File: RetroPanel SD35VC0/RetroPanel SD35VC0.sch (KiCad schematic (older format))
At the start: 20 parts, among them J1 Front Panel, J2 SD35VC0, J3 IDE, J4 GND, J5 +5V, J7 POWER, M1 Mounting_Pin, M10 Mounting_Pad, M11 Mounting_Pad, M12 Mounting_Pad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

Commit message: SD35VC0 Front sketched out
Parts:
- added J10: LED_POWER, RetroPanel:PinHeader_1x02_P2.54mm_Vertical, symbol Connector_Generic:Conn_01x02
- added J6: SW_TURBO, RetroPanel:PinHeader_1x02_P2.54mm_Vertical, symbol Connector_Generic:Conn_01x02
- added J8: LED_TURBO, RetroPanel:PinHeader_1x02_P2.54mm_Vertical, symbol Connector_Generic:Conn_01x02
- added J9: SW_POWER, RetroPanel:PinHeader_1x02_P2.54mm_Vertical, symbol Connector_Generic:Conn_01x02
- added R1, R2: 0, resistor:R_Axial_DIN0207_L6.3mm_D2.5mm_P10.16mm_Horizontal, symbol Device:R_Small
- J1: footprint RetroPanel:Module_Panel -> RetroPanel:SD35VC0_Module_Panel; symbol RetroPanel:Front_Panel -> RetroPanel:SD35VC0_Front_Panel
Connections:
- net LED_HDD1 is gone; now on net LED_TURBO1: J1.22 (LED_TURBO1)
- net LED_HDD2 is gone; now on net LED_TURBO2: J1.23 (LED_TURBO2)
- net SW_EXTRA1 is gone; now on net SW_TURBO1: J1.24 (SW_TURBO1)
- net SW_EXTRA2 is gone; now on net SW_TURBO2: J1.25 (SW_TURBO2)
- net SW_RESET1 is gone; now on net LED_PWR1: J1.8 (LED_PWR1)
- net SW_RESET2 is gone; now on net LED_PWR2: J1.9 (LED_PWR2)
- net +5V: now also J1.30 (VCC), J5.1 (Pin_1), J7.4 (Pin_4); no longer J1.1 (VCC)
- net GND: now also J1.1 (GND); no longer J1.30 (GND)
- net LED_PWR1: now also R2.2; no longer J1.6 (LED_PWR1)
- net LED_PWR2: now also J10.2 (Pin_2); no longer J1.7 (LED_PWR2)
- net LED_TURBO1: now also R1.2; no longer J1.28 (LED_TURBO1)
- net LED_TURBO2: now also J8.2 (Pin_2); no longer J1.29 (LED_TURBO2)
- net SW_PWR1: now also J1.6 (SW_PWR1), J9.1 (Pin_1); no longer J1.4 (SW_PWR1)
- net SW_PWR2: now also J1.7 (SW_PWR2), J9.2 (Pin_2); no longer J1.5 (SW_PWR2)
- net SW_TURBO1: now also J6.1 (Pin_1); no longer J1.26 (SW_TURBO1)
- net SW_TURBO2: now also J6.2 (Pin_2); no longer J1.27 (SW_TURBO2)
- new net: J8.1 (Pin_1), R1.1
- new net: J10.1 (Pin_1), R2.1
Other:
- moved on the sheet: J2, J3, J4, J5, J7

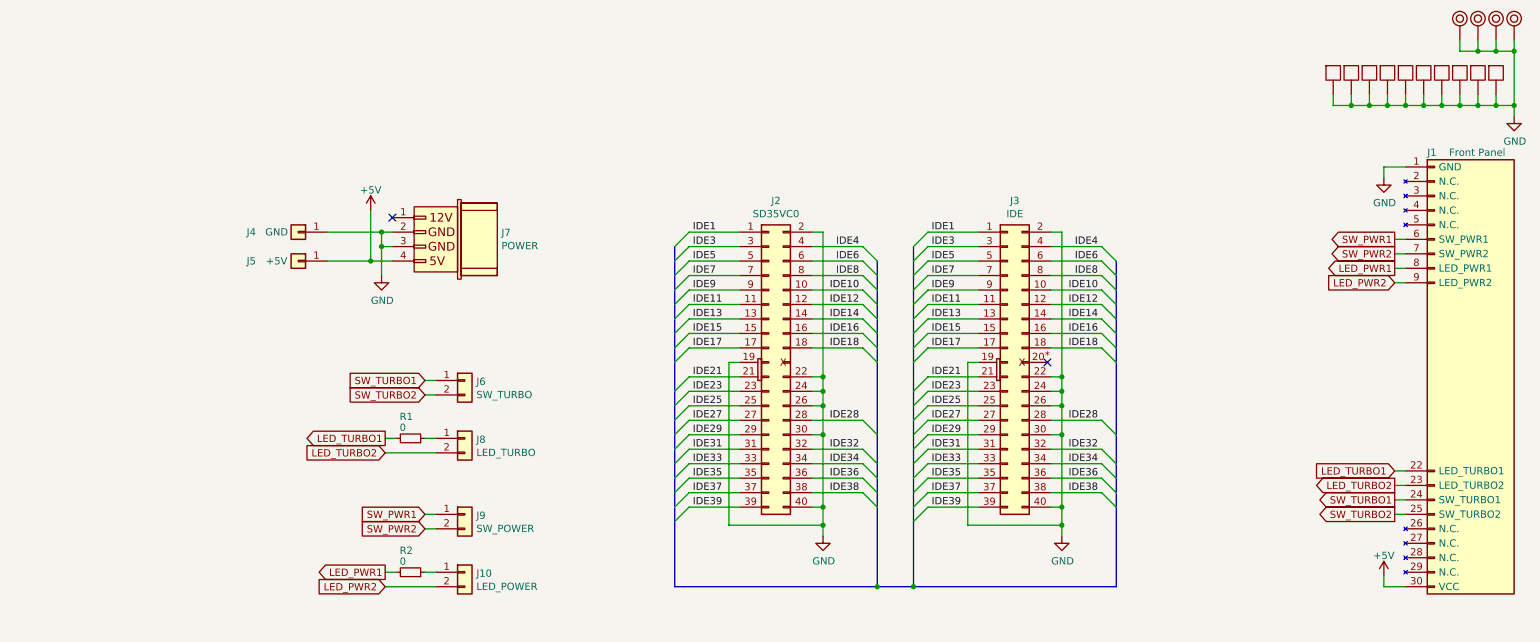
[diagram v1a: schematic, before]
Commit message: Changed SW_PWR to pads for cable as it probably should be
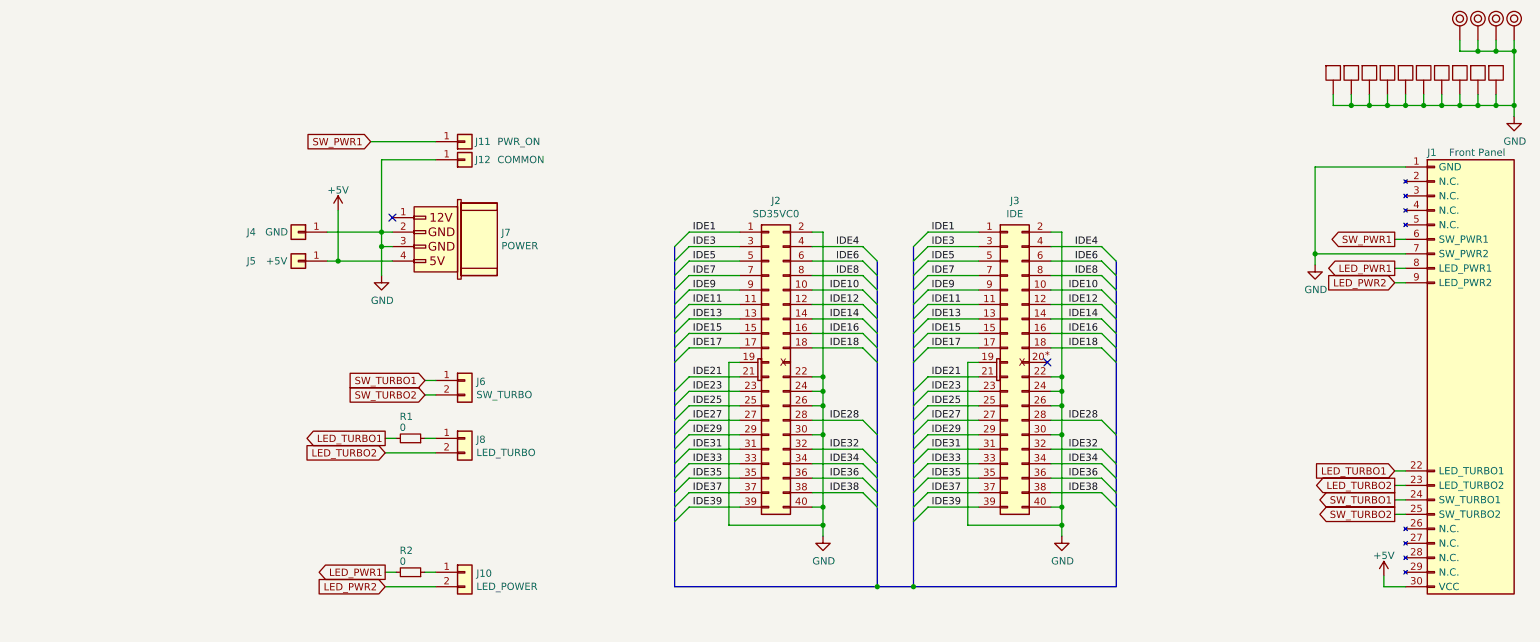
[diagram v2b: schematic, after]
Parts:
- removed J9: SW_POWER, RetroPanel:PinHeader_1x02_P2.54mm_Vertical, symbol Connector_Generic:Conn_01x02
- added J11: PWR_ON, RetroPanel:PSU_Wire, symbol Connector_Generic:Conn_01x01
- added J12: COMMON, RetroPanel:PSU_Wire, symbol Connector_Generic:Conn_01x01
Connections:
- net SW_PWR2 is gone; now on net GND: J1.7 (SW_PWR2)
- net GND: now also J12.1 (Pin_1)
- net SW_PWR1: now also J11.1 (Pin_1)
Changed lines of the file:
@@
 L power:GND #PWR0101
 U 1 1 6282785A
-P 10175 1725
-F 0 "#PWR0101" H 10175 1475 50  0001 C CNN
-F 1 "GND" H 10180 1552 50  0000 C CNN
-F 2 "" H 10175 1725 50  0001 C CNN
-F 3 "" H 10175 1725 50  0001 C CNN
-	1    10175 1725
+P 9700 2325
+F 0 "#PWR0101" H 9700 2075 50  0001 C CNN
+F 1 "GND" H 9705 2152 50  0000 C CNN
+F 2 "" H 9700 2325 50  0001 C CNN
+F 3 "" H 9700 2325 50  0001 C CNN
+	1    9700 2325
 	1    0    0    -1
 $EndComp
 Wire Wire Line
 	10175 4475 10175 4550
-Wire Wire Line
-	10175 1650 10175 1725
 Text GLabel 10250 2150 0    50   Output ~ 0
 SW_PWR1
-Text GLabel 10250 2250 0    50   Output ~ 0
-SW_PWR2
 Text GLabel 10250 2350 0    50   Output ~ 0
 LED_PWR1
@@
 Text GLabel 10250 3850 0    50   Output ~ 0
 LED_TURBO2
-Wire Wire Line
-	10250 2150 10325 2150
-Wire Wire Line
-	10250 2250 10325 2250
-Wire Wire Line
-	10250 2350 10325 2350
-Wire Wire Line
-	10250 2450 10325 2450
 Wire Wire Line
 	10250 3950 10325 3950
@@
 Connection ~ 3250 2100
 Wire Wire Line
-	2875 2300 3175 2300
-Wire Wire Line
-	10175 1650 10325 1650
+	2875 2300 2950 2300
 $Comp
 L RetroPanel:SD35VC0_Front_Panel J1
@@
 Wire Wire Line
 	3550 3525 3625 3525
-Text GLabel 3550 4050 0    50   Input ~ 0
+Text GLabel 3175 1475 0    50   Input ~ 0
 SW_PWR1
-Text GLabel 3550 4150 0    50   Input ~ 0
-SW_PWR2
-$Comp
-L Connector_Generic:Conn_01x02 J9
-U 1 1 635DD778
-P 3825 4050
-F 0 "J9" H 3905 4042 50  0000 L CNN
-F 1 "SW_POWER" H 3905 3951 50  0000 L CNN
-F 2 "RetroPanel:PinHeader_1x02_P2.54mm_Vertical" H 3825 4050 50  0001 C CNN
-F 3 "~" H 3825 4050 50  0001 C CNN
-	1    3825 4050
-	1    0    0    -1
-$EndComp
-Wire Wire Line
-	3550 4050 3625 4050
-Wire Wire Line
-	3550 4150 3625 4150
 $Comp
 L Device:R_Small R1
@@
 L power:+5V #PWR0105
 U 1 1 6403A47A
-P 3175 1950
-F 0 "#PWR0105" H 3175 1800 50  0001 C CNN
-F 1 "+5V" H 3175 2090 50  0000 C CNN
-F 2 "" H 3175 1950 50  0000 C CNN
-F 3 "" H 3175 1950 50  0000 C CNN
-	1    3175 1950
-	1    0    0    -1
-$EndComp
-Wire Wire Line
-	3175 1950 3175 2300
-Connection ~ 3175 2300
-Wire Wire Line
-	3175 2300 3325 2300
+P 2950 1950
+F 0 "#PWR0105" H 2950 1800 50  0001 C CNN
+F 1 "+5V" H 2950 2090 50  0000 C CNN
+F 2 "" H 2950 1950 50  0000 C CNN
+F 3 "" H 2950 1950 50  0000 C CNN
+	1    2950 1950
+	1    0    0    -1
+$EndComp
+Wire Wire Line
+	2950 1950 2950 2300
+$Comp
+L Connector_Generic:Conn_01x01 J12
+U 1 1 63D935B1
+P 3825 1600
+F 0 "J12" H 3950 1600 50  0000 C CNN
+F 1 "COMMON" H 4050 1600 50  0000 L CNN
+F 2 "RetroPanel:PSU_Wire" H 3825 1600 50  0001 C CNN
+F 3 "~" H 3825 1600 50  0001 C CNN
+	1    3825 1600
+	1    0    0    1
+$EndComp
+$Comp
+L Connector_Generic:Conn_01x01 J11
+U 1 1 63D95DEE
+P 3825 1475
+F 0 "J11" H 3950 1475 50  0000 C CNN
+F 1 "PWR_ON" H 4050 1475 50  0000 L CNN
+F 2 "RetroPanel:PSU_Wire" H 3825 1475 50  0001 C CNN
+F 3 "~" H 3825 1475 50  0001 C CNN
+	1    3825 1475
+	1    0    0    1
+$EndComp
+Connection ~ 2950 2300
+Wire Wire Line
+	2950 2300 3325 2300
+Wire Wire Line
+	3250 1600 3250 2100
+Wire Wire Line
+	3250 1600 3625 1600
+Wire Wire Line
+	3175 1475 3625 1475
+Wire Wire Line
+	10250 2150 10325 2150
+Wire Wire Line
+	10325 2350 10250 2350
+Wire Wire Line
+	10250 2450 10325 2450
+Wire Wire Line
+	10325 2250 9700 2250
+Wire Wire Line
+	9700 2250 9700 2325
+Wire Wire Line
+	9700 2250 9700 1650
+Connection ~ 9700 2250
+Wire Wire Line
+	9700 1650 10325 1650
 Wire Bus Line
 	6675 2300 6675 4550
